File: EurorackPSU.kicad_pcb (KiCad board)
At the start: 4 copper layers, 127 x 152.4 mm, 42 parts, among them J2 Conn_01x03_Male, J4 Conn_01x03_Male, U1 lt8638s, U2 lt8638s

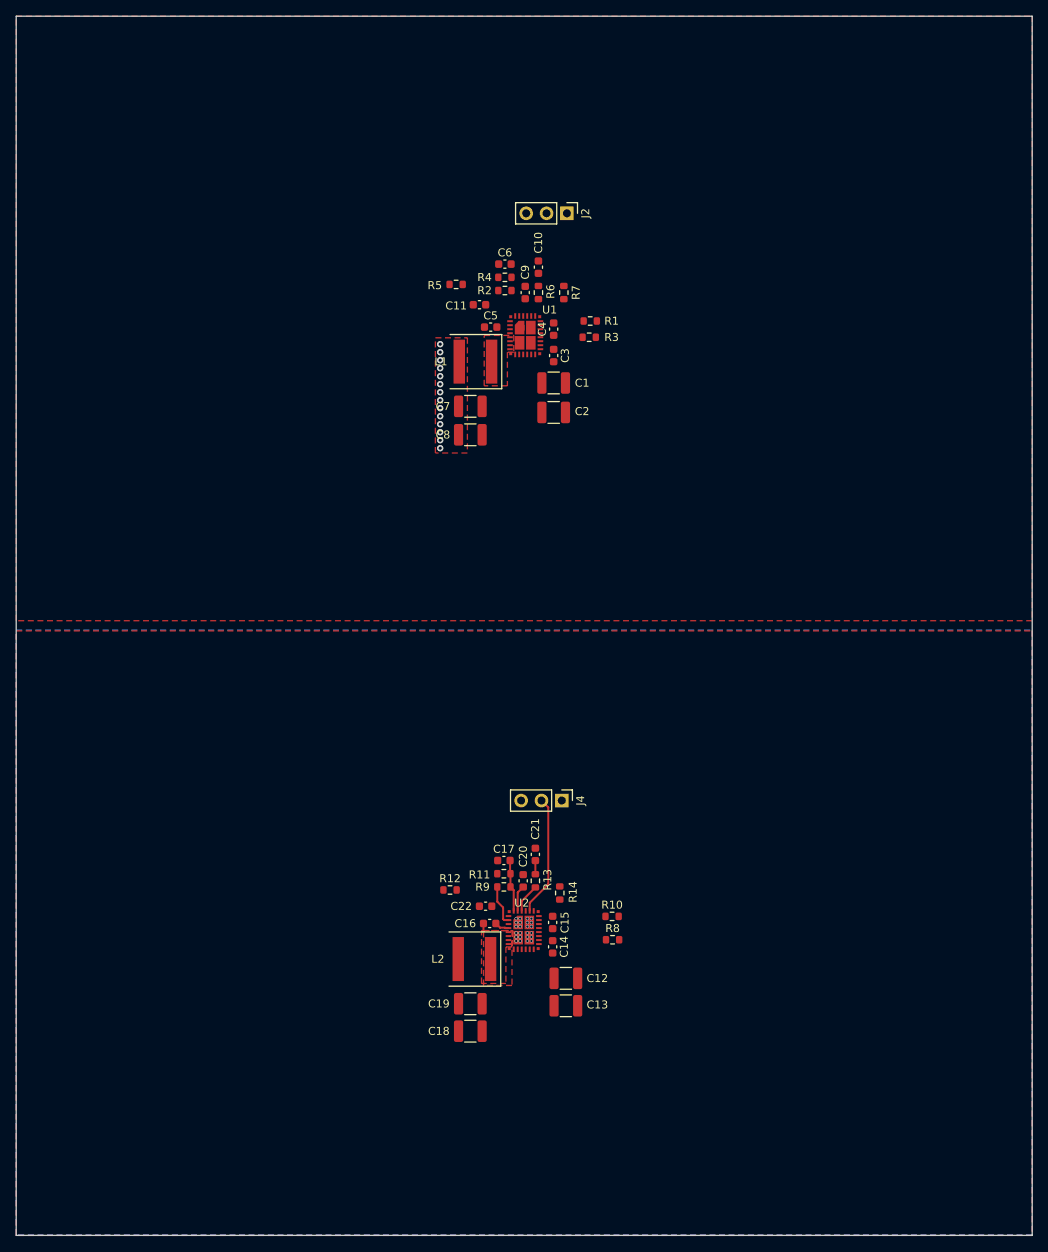
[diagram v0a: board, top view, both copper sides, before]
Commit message: Routing signals for the +12v regulator
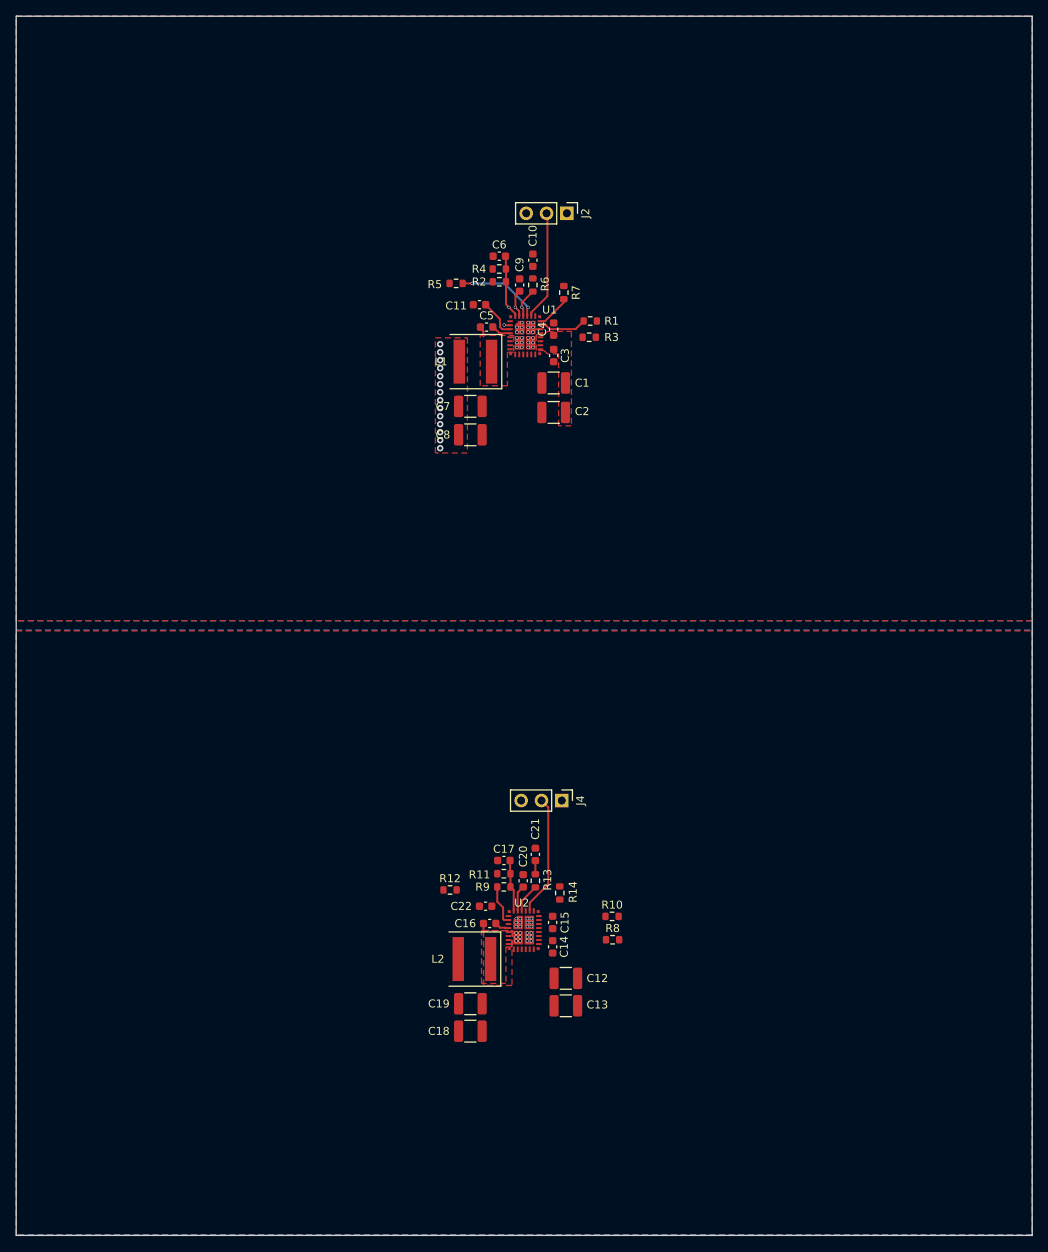
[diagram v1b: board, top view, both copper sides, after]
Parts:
- moved R2 1.29 mm to (85.8, 58.6)
- moved R4 1.25 mm to (85.8, 57.0)
- moved C6 1.21 mm to (85.8, 55.4)
- moved C9 1.18 mm to (88.3, 59.0)
- moved R6 1.18 mm to (90.0, 59.0)
- moved C10 1.12 mm to (90.0, 55.9)
- moved C5 0.51 mm to (84.2, 64.3)
- moved R5 0.13 mm to (80.4, 58.8)
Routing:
- net Net-(J2-Pad2): track 0.00 -> 13.7 mm
- net Net-(R5-Pad2): track 0.00 -> 10.6 mm, vias 0 -> 2
- net Net-(C6-Pad2): track 0.00 -> 7.98 mm, vias 0 -> 1
- net Net-(R1-Pad2): track 0.00 -> 6.03 mm
- net Net-(C11-Pad1): track 0.00 -> 4.89 mm
- net Net-(R7-Pad1): track 0.00 -> 4.30 mm
- net Net-(R6-Pad1): track 0.00 -> 3.70 mm, vias 0 -> 1
- net Net-(C9-Pad1): track 0.00 -> 3.52 mm, vias 0 -> 1
- net Net-(C5-Pad2): track 0.00 -> 2.47 mm
- net Net-(C5-Pad1): track 0.00 -> 1.29 mm
- net GND: track 5.05 -> 6.33 mm, vias 0 -> 23
- net +12V: track 0.00 -> 0.74 mm, vias 14 -> 15
- added copper zone on B.Cu, net GND
- added copper zone on F.Cu, net Net-(C1-Pad1)

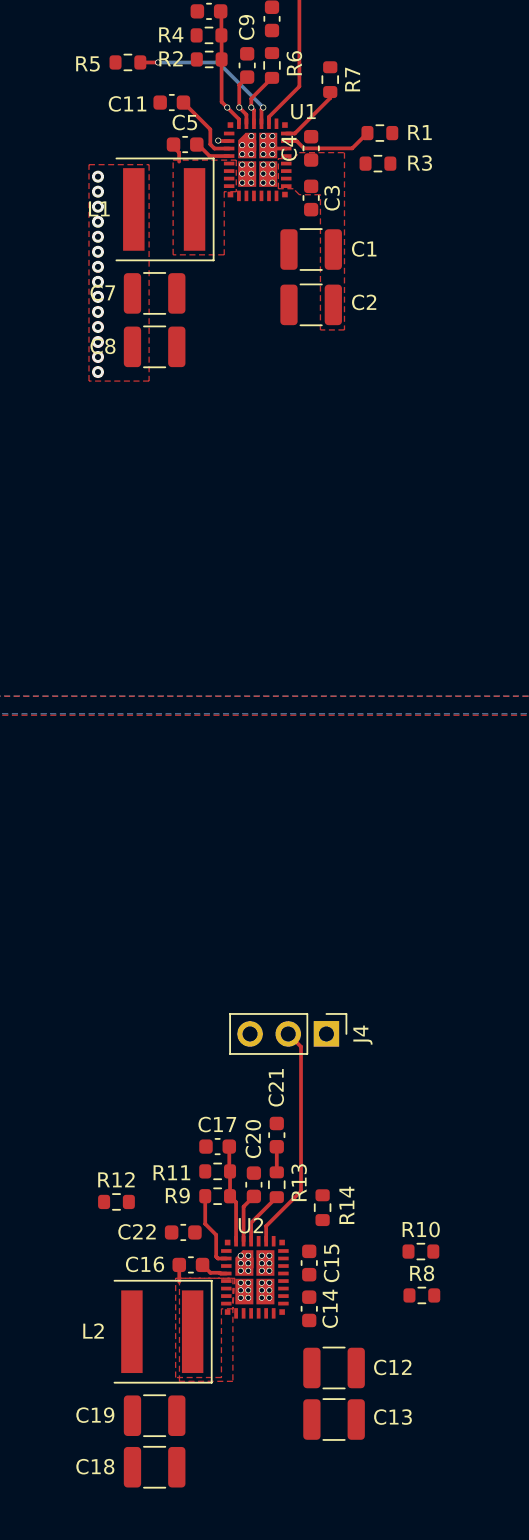
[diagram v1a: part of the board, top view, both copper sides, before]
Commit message: Routing signals for the -12v regulator
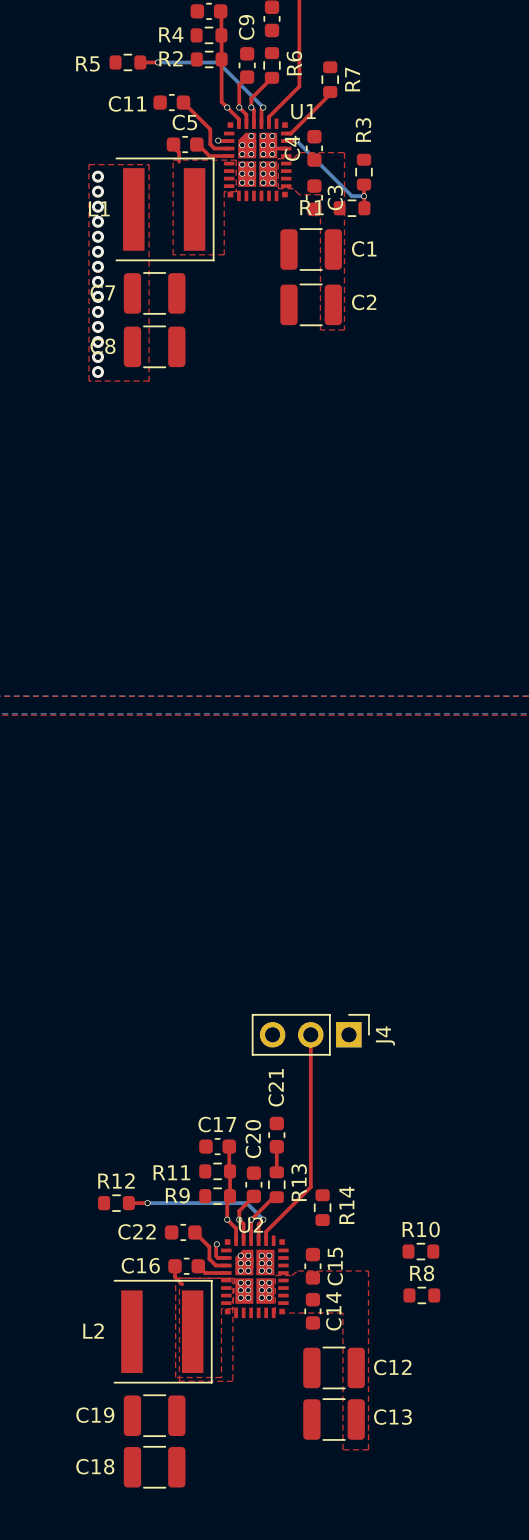
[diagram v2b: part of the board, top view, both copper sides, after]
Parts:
- moved R1 5.33 mm to (95.3, 68.5), turned to 0 degrees
- moved J4 1.50 mm to (95.1, 123.5)
- moved R3 1.09 mm to (96.1, 66.1), turned to 90 degrees
- moved C15 0.33 mm to (92.7, 138.9)
- moved C14 0.30 mm to (92.7, 141.9)
- moved C16 0.30 mm to (84.3, 138.9)
- moved C3 0.22 mm to (92.8, 67.8)
- moved C4 0.22 mm to (92.8, 64.5)
- moved R12 0.08 mm to (79.6, 134.7)
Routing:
- net Net-(R12-Pad2): track 0.00 -> 10.9 mm, vias 0 -> 2
- net GND: track 6.33 -> 2.82 mm, vias 23 -> 24
- net Net-(C22-Pad1): track 0.00 -> 3.47 mm
- net Net-(R1-Pad2): track 6.03 -> 8.30 mm, vias 0 -> 2
- net Net-(C20-Pad1): track 3.27 -> 3.47 mm, vias 0 -> 1
- net Net-(C17-Pad2): track 6.48 -> 6.60 mm, vias 0 -> 1
- net Net-(R13-Pad1): track 3.64 -> 3.72 mm, vias 0 -> 1

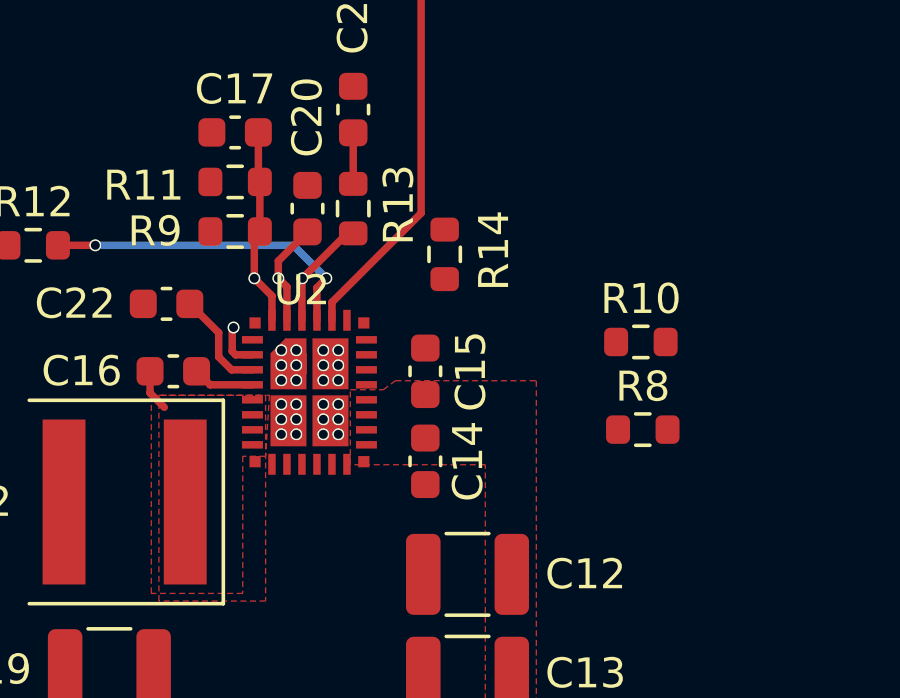
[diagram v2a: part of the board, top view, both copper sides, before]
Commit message: More signal routing
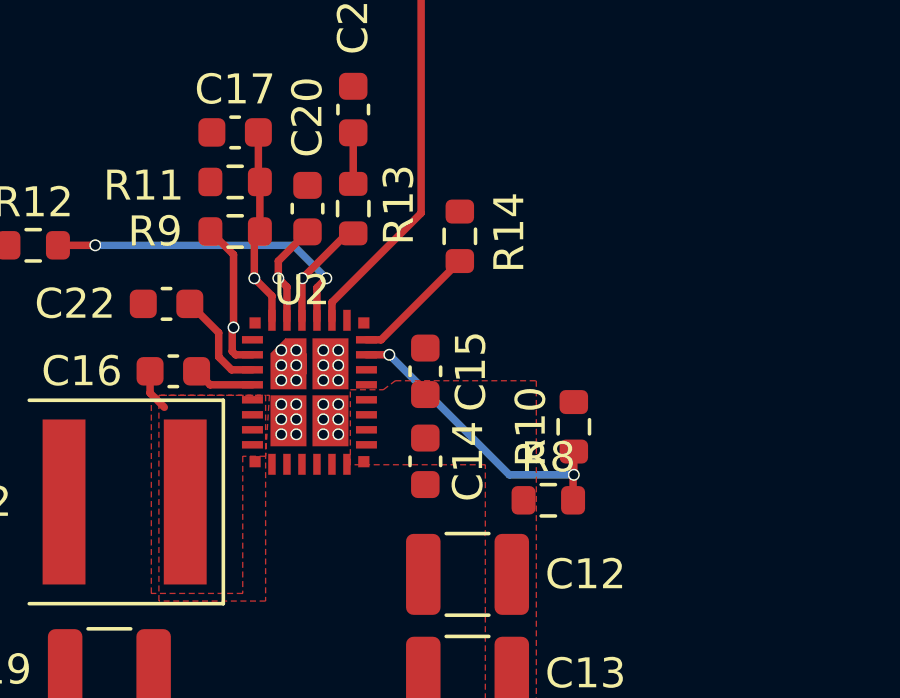
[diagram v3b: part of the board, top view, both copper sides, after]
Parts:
- moved R8 3.93 mm to (96.8, 143.2)
- moved R10 3.60 mm to (97.7, 140.8), turned to 90 degrees
- moved R14 0.79 mm to (93.8, 134.4)
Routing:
- net Net-(R10-Pad1): track 0.00 -> 10.2 mm, vias 0 -> 2
- net Net-(R14-Pad1): track 0.00 -> 4.20 mm
- net GND: track 2.82 -> 6.34 mm

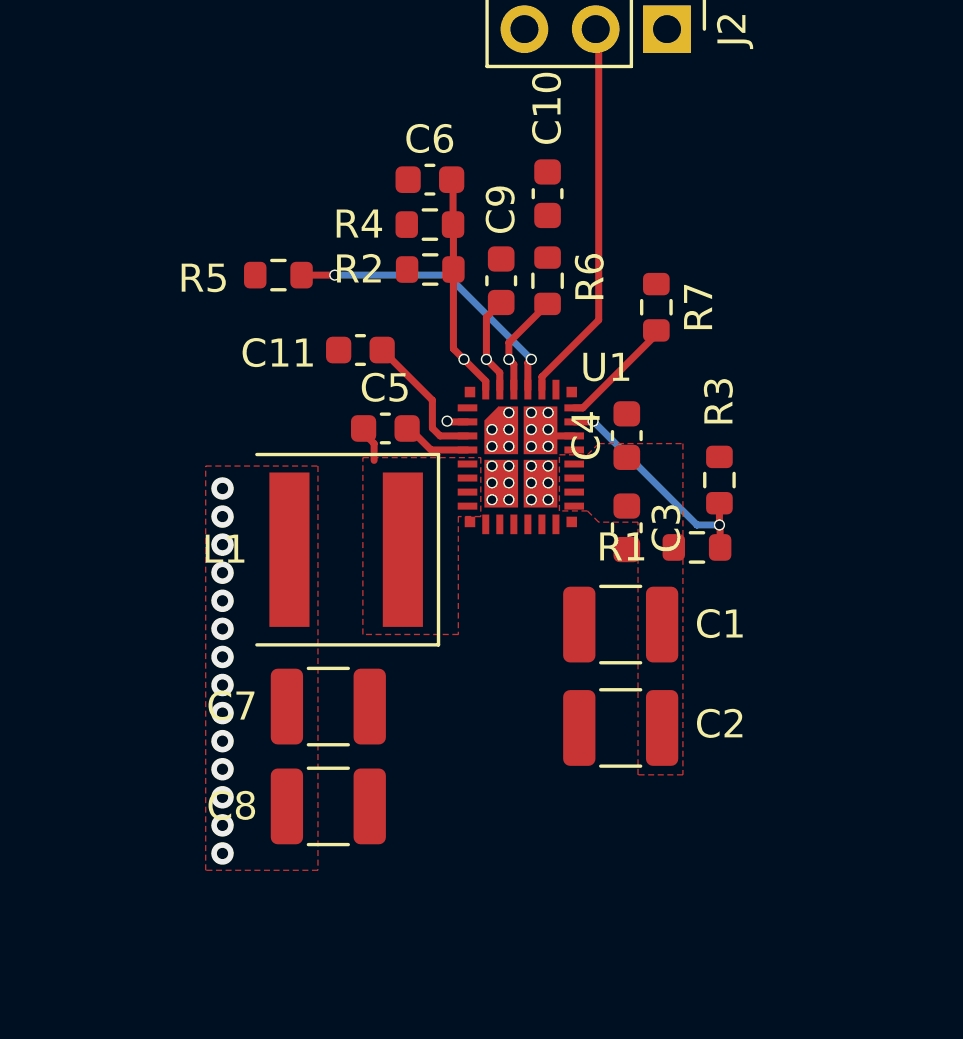
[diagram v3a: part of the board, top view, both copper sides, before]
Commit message: Assigned connectors for power input and output, and exported the netlist again
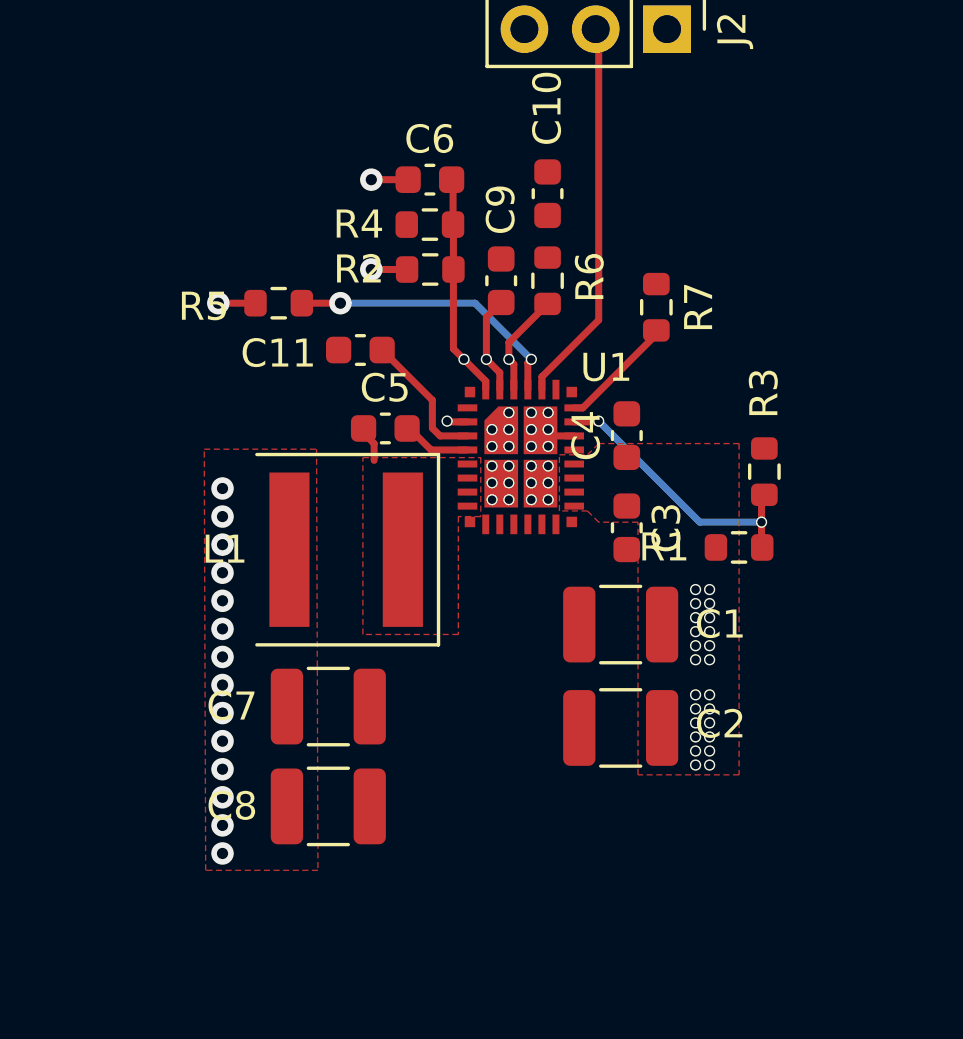
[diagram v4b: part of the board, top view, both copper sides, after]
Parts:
- moved R3 1.63 mm to (97.7, 65.8)
- moved R1 1.50 mm to (96.8, 68.5)
- moved R5 1.00 mm to (80.4, 59.8)
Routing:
- net +12V: track 0.74 -> 4.65 mm, vias 15 -> 18
- net Net-(R1-Pad2): track 8.30 -> 10.3 mm
- net Net-(C1-Pad1): vias 0 -> 24
- added copper zone on In2.Cu, net Net-(C1-Pad1)
